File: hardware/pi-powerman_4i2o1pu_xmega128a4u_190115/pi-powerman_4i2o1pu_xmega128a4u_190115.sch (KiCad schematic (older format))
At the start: 93 parts, among them J1 Vin: +[16, 24]V, J2 UPS_in, J3 UPS_out, J4 AVR-PDI-6, J5 +5V OUT1, J7 +5V OUT2, J8 UPS_status, J9 UPS_bat, Q1 IRLML6402, Q2 BSS138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

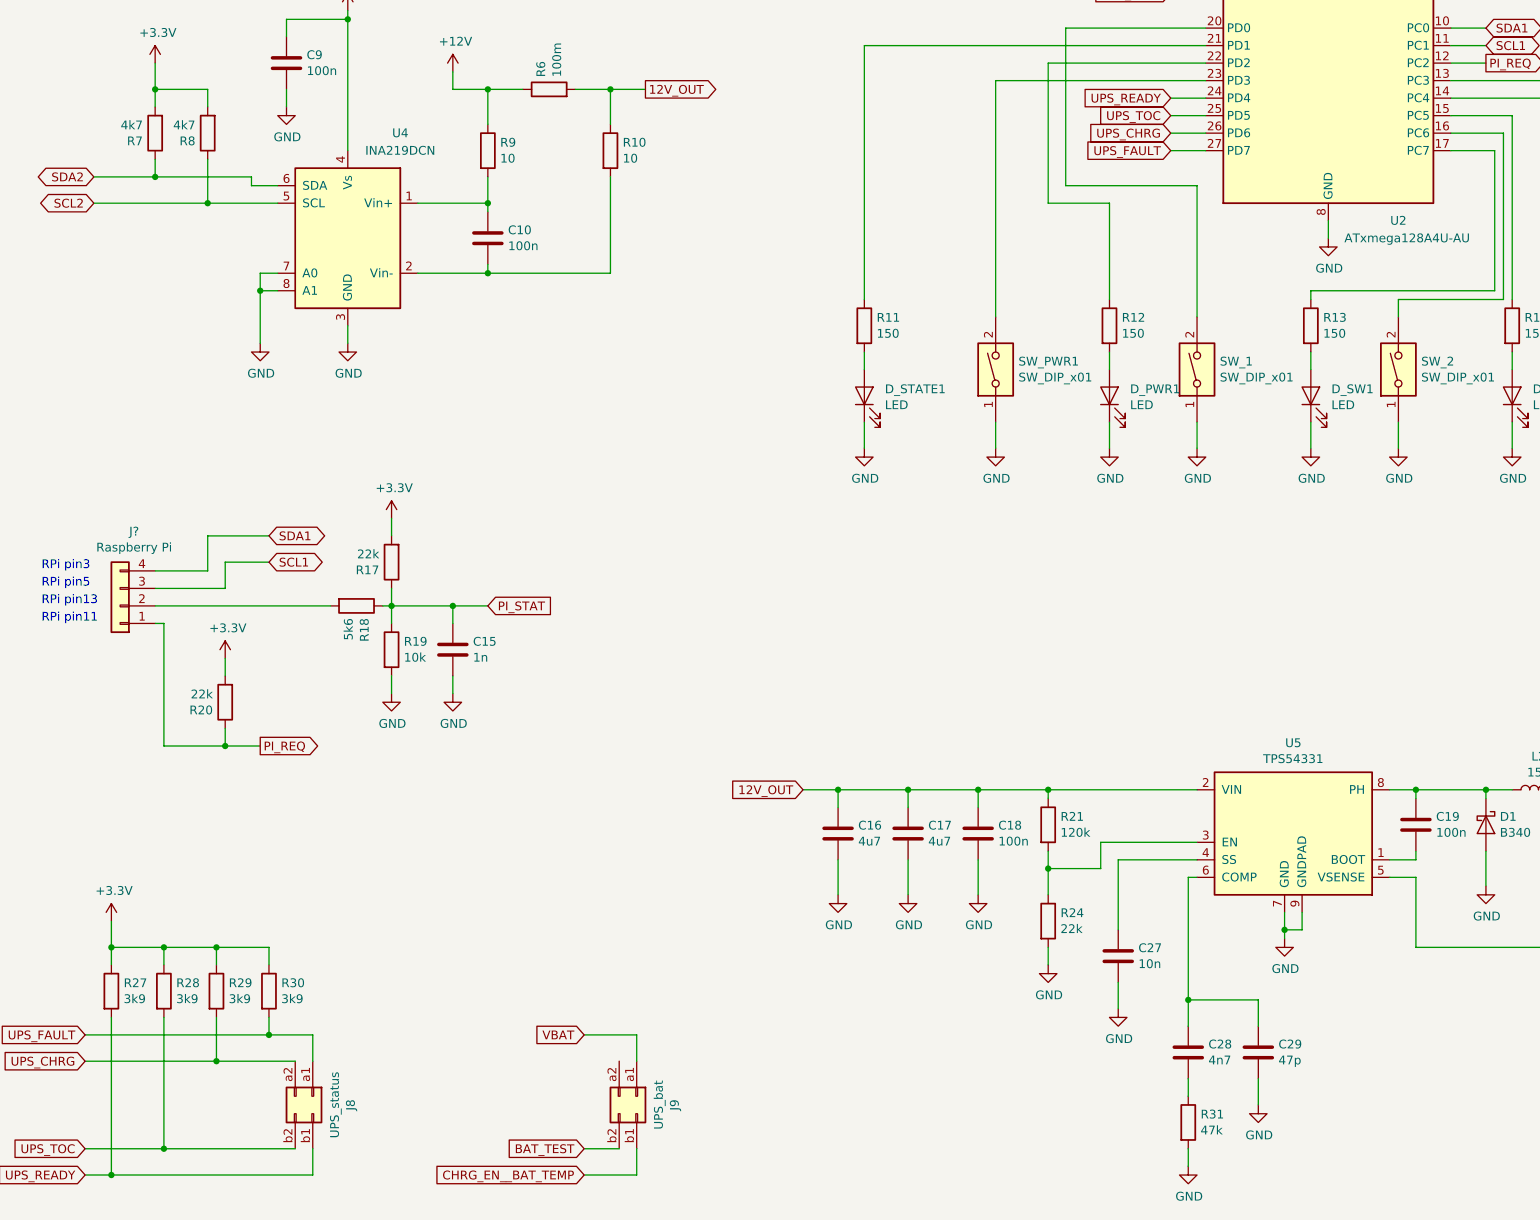
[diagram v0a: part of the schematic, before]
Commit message: symbols update
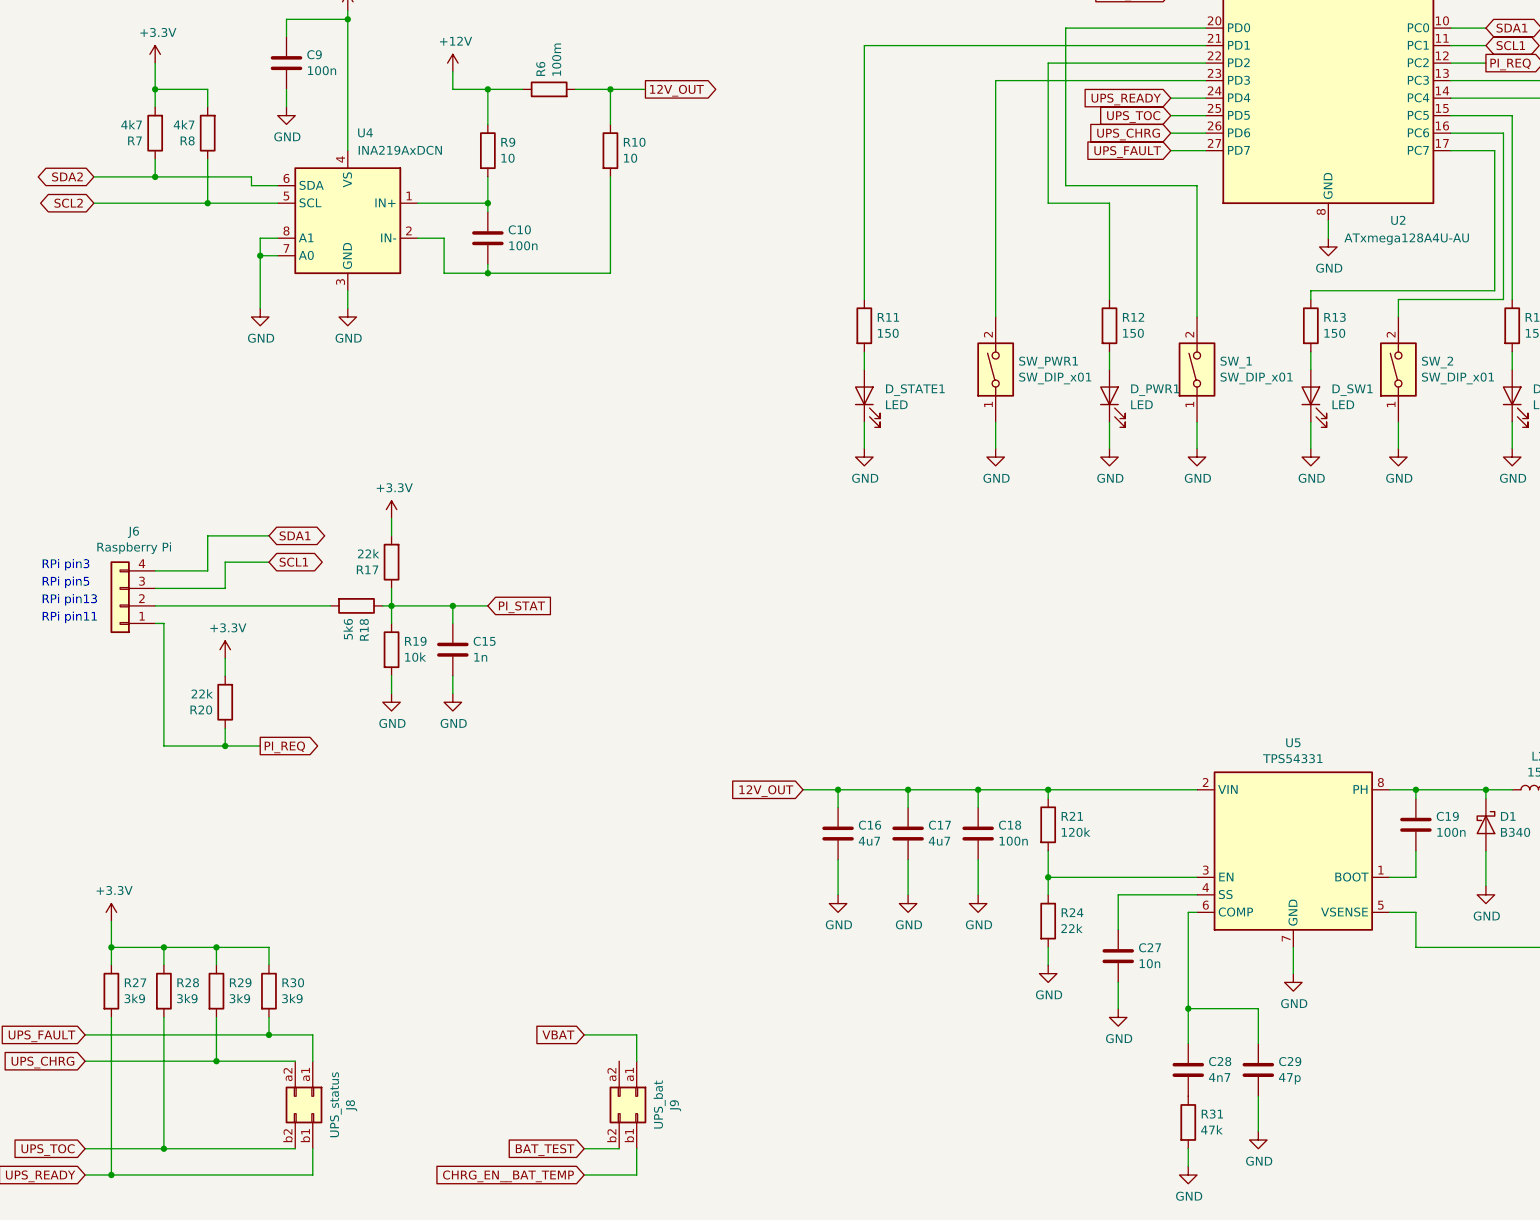
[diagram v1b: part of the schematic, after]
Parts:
- removed U4: INA219DCN, symbol ina219dcn:INA219DCN
- removed U5: TPS54331, symbol tps54331:TPS54331
- added U4: INA219AxDCN, Package_TO_SOT_SMD:SOT-23-8, symbol Analog_ADC:INA219AxDCN
- added U5: TPS54331, Package_SO:SOIC-8_3.9x4.9mm_P1.27mm, symbol obbo_IC:TPS54331
- U2: footprint Housings_QFP:TQFP-44_10x10mm_Pitch0.8mm -> Package_QFP:TQFP-44_10x10mm_P0.8mm
- gave numbers to parts that had none: 1
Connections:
- net +3V3: now also U4.4 (VS)
- net 12V_OUT: now also U5.2 (VIN)
- net GND: now also U4.3 (GND), U4.7 (A0), U4.8 (A1), U5.7 (GND)
- net SCL2: now also U4.5 (SCL)
- net SDA2: now also U4.6 (SDA)
- net at R23.2, R25.1, R26.1: now also U5.5 (VSENSE)
- net at C19.1, D1.1 (K), L2.1: now also U5.8 (PH)
- net at C19.2: now also U5.1 (BOOT)
- net at C28.1, C29.1: now also U5.6 (COMP)
- net at C27.1: now also U5.4 (SS)
- net at R21.2, R24.1: now also U5.3 (EN)
- net at C10.1, R9.2: now also U4.1 (IN+)
- net at C10.2, R10.2: now also U4.2 (IN-)
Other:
- moved on the sheet: C28, C29
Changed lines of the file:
@@
 EESchema Schematic File Version 4
 LIBS:pi-powerman_4i2o1pu_xmega128a4u_190115-cache
-EELAYER 26 0
+EELAYER 30 0
 EELAYER END
 $Descr A3 16535 11693
@@
 $EndDescr
 $Comp
-L MCU_Microchip_ATmega:ATxmega128A4U-AU U2
-U 1 1 5C9A9842
-P 8650 3550
-F 0 "U2" H 9050 2150 50  0000 C CNN
-F 1 "ATxmega128A4U-AU" H 9100 2050 50  0000 C CNN
-F 2 "Housings_QFP:TQFP-44_10x10mm_Pitch0.8mm" H 8650 3550 50  0001 C CIN
-F 3 "http://ww1.microchip.com/downloads/en/DeviceDoc/Atmel-8387-8-and16-bit-AVR-Microcontroller-XMEGA-A4U_Datasheet.pdf" H 8650 3550 50  0001 C CNN
-	1    8650 3550
-	1    0    0    -1
-$EndComp
-$Comp
 L Regulator_Linear:LM1117-3.3 U3
 U 1 1 5C9A9A34
@@
 L Device:C C29
 U 1 1 5C9AE2DB
-P 8250 9700
-F 0 "C29" H 8365 9746 50  0000 L CNN
-F 1 "47p" H 8365 9655 50  0000 L CNN
-F 2 "Resistors_SMD:R_0805_HandSoldering" H 8288 9550 50  0001 C CNN
-F 3 "~" H 8250 9700 50  0001 C CNN
-	1    8250 9700
+P 8250 9800
+F 0 "C29" H 8365 9846 50  0000 L CNN
+F 1 "47p" H 8365 9755 50  0000 L CNN
+F 2 "Resistors_SMD:R_0805_HandSoldering" H 8288 9650 50  0001 C CNN
+F 3 "~" H 8250 9800 50  0001 C CNN
+	1    8250 9800
 	1    0    0    -1
 $EndComp
@@
 L Device:C C28
 U 1 1 5C9AE33F
-P 7850 9700
-F 0 "C28" H 7965 9746 50  0000 L CNN
-F 1 "4n7" H 7965 9655 50  0000 L CNN
-F 2 "Resistors_SMD:R_0805_HandSoldering" H 7888 9550 50  0001 C CNN
-F 3 "~" H 7850 9700 50  0001 C CNN
-	1    7850 9700
+P 7850 9800
+F 0 "C28" H 7965 9846 50  0000 L CNN
+F 1 "4n7" H 7965 9755 50  0000 L CNN
+F 2 "Resistors_SMD:R_0805_HandSoldering" H 7888 9650 50  0001 C CNN
+F 3 "~" H 7850 9800 50  0001 C CNN
+	1    7850 9800
 	1    0    0    -1
 $EndComp
@@
 $EndComp
 $Comp
-L tps54331:TPS54331 U5
-U 1 1 5C9FF6F5
-P 8450 8400
-F 0 "U5" H 8450 8867 50  0000 C CNN
-F 1 "TPS54331" H 8450 8776 50  0000 C CNN
-F 2 "" H 8400 8400 50  0001 C CNN
-F 3 "" H 8400 8400 50  0001 C CNN
-	1    8450 8400
-	1    0    0    -1
-$EndComp
-$Comp
 L power:GND #PWR075
 U 1 1 5CA013F7
@@
 L power:GND #PWR070
 U 1 1 5CA0163B
-P 8400 9050
-F 0 "#PWR070" H 8400 8800 50  0001 C CNN
-F 1 "GND" H 8405 8877 50  0000 C CNN
-F 2 "" H 8400 9050 50  0001 C CNN
-F 3 "" H 8400 9050 50  0001 C CNN
-	1    8400 9050
+P 8450 9250
+F 0 "#PWR070" H 8450 9000 50  0001 C CNN
+F 1 "GND" H 8455 9077 50  0000 C CNN
+F 2 "" H 8450 9250 50  0001 C CNN
+F 3 "" H 8450 9250 50  0001 C CNN
+	1    8450 9250
 	1    0    0    -1
 $EndComp
@@
 L power:GND #PWR074
 U 1 1 5CA0168C
-P 8250 10000
-F 0 "#PWR074" H 8250 9750 50  0001 C CNN
-F 1 "GND" H 8255 9827 50  0000 C CNN
-F 2 "" H 8250 10000 50  0001 C CNN
-F 3 "" H 8250 10000 50  0001 C CNN
-	1    8250 10000
+P 8250 10150
+F 0 "#PWR074" H 8250 9900 50  0001 C CNN
+F 1 "GND" H 8255 9977 50  0000 C CNN
+F 2 "" H 8250 10150 50  0001 C CNN
+F 3 "" H 8250 10150 50  0001 C CNN
+	1    8250 10150
 	1    0    0    -1
 $EndComp
@@
 	7050 8200 6650 8200
 Wire Wire Line
-	7050 8550 7050 8650
+	7050 8550 7050 8700
 Wire Wire Line
 	7050 9100 7050 9200
@@
 Wire Wire Line
 	5850 8600 5850 8800
-Wire Wire Line
-	7900 8500 7350 8500
-Wire Wire Line
-	7350 8500 7350 8650
-Wire Wire Line
-	7350 8650 7050 8650
-Connection ~ 7050 8650
-Wire Wire Line
-	7050 8650 7050 8800
-Wire Wire Line
-	7900 8600 7450 8600
-Wire Wire Line
-	7450 8600 7450 9000
-Wire Wire Line
-	8250 9400 7850 9400
+Connection ~ 7050 8700
+Wire Wire Line
+	7050 8700 7050 8800
+Wire Wire Line
+	7900 8800 7450 8800
+Wire Wire Line
+	7450 8800 7450 9000
+Wire Wire Line
+	8250 9450 7850 9450
 Wire Wire Line
 	7450 9300 7450 9450
 Wire Wire Line
-	7850 9850 7850 9950
-Wire Wire Line
-	8250 9850 8250 10000
+	8250 9950 8250 10150
 Wire Wire Line
 	7850 10250 7850 10350
-Wire Wire Line
-	8400 8900 8400 9000
-Wire Wire Line
-	8500 8900 8500 9000
-Wire Wire Line
-	8500 9000 8400 9000
-Connection ~ 8400 9000
-Wire Wire Line
-	8400 9000 8400 9050
 Wire Wire Line
 	9000 8200 9150 8200
@@
 	9150 8200 9550 8200
 Wire Wire Line
-	9150 8550 9150 8600
-Wire Wire Line
-	9150 8600 9000 8600
+	9150 8550 9150 8700
+Wire Wire Line
+	9150 8700 9000 8700
 Wire Wire Line
 	9550 8550 9550 8750
@@
 	11100 9100 9150 9100
 Wire Wire Line
-	9150 9100 9150 8700
-Wire Wire Line
-	9150 8700 9000 8700
+	9150 9100 9150 8900
+Wire Wire Line
+	9150 8900 9000 8900
 Connection ~ 11250 9000
 $Comp
@@
 Wire Wire Line
 	1950 4200 1950 4050
-$Comp
-L ina219dcn:INA219DCN U4
-U 1 1 5CE81E04
-P 3050 5050
-F 0 "U4" H 3350 5650 50  0000 C CNN
-F 1 "INA219DCN" H 3350 5550 50  0000 C CNN
-F 2 "" H 3050 5050 50  0001 C CNN
-F 3 "" H 3050 5050 50  0001 C CNN
-	1    3050 5050
-	1    0    0    -1
-$EndComp
 Wire Wire Line
 	2250 4850 2650 4850
@@
 L power:GND #PWR033
 U 1 1 5CEC82A7
-P 3050 5650
-F 0 "#PWR033" H 3050 5400 50  0001 C CNN
-F 1 "GND" H 3055 5477 50  0000 C CNN
-F 2 "" H 3050 5650 50  0001 C CNN
-F 3 "" H 3050 5650 50  0001 C CNN
-	1    3050 5650
+P 3050 5450
+F 0 "#PWR033" H 3050 5200 50  0001 C CNN
+F 1 "GND" H 3055 5277 50  0000 C CNN
+F 2 "" H 3050 5450 50  0001 C CNN
+F 3 "" H 3050 5450 50  0001 C CNN
+	1    3050 5450
 	1    0    0    -1
 $EndComp
@@
 L power:GND #PWR032
 U 1 1 5CEF341C
-P 2550 5650
-F 0 "#PWR032" H 2550 5400 50  0001 C CNN
-F 1 "GND" H 2555 5477 50  0000 C CNN
-F 2 "" H 2550 5650 50  0001 C CNN
-F 3 "" H 2550 5650 50  0001 C CNN
-	1    2550 5650
+P 2550 5450
+F 0 "#PWR032" H 2550 5200 50  0001 C CNN
+F 1 "GND" H 2555 5277 50  0000 C CNN
+F 2 "" H 2550 5450 50  0001 C CNN
+F 3 "" H 2550 5450 50  0001 C CNN
+	1    2550 5450
 	1    0    0    -1
 $EndComp
@@
 	3050 3800 3050 3750
 Wire Wire Line
-	2550 5650 2550 5350
-Wire Wire Line
-	2550 5250 2650 5250
-Wire Wire Line
-	2650 5350 2550 5350
-Connection ~ 2550 5350
-Wire Wire Line
-	2550 5350 2550 5250
-Wire Wire Line
-	3050 5550 3050 5650
+	2550 5450 2550 5150
+Wire Wire Line
+	2550 5050 2650 5050
+Wire Wire Line
+	2650 5150 2550 5150
+Connection ~ 2550 5150
+Wire Wire Line
+	2550 5150 2550 5050
+Wire Wire Line
+	3050 5350 3050 5450
 $Comp
 L Device:C C10
@@
 	3850 4900 3850 4850
 Connection ~ 3850 4850
-Wire Wire Line
-	3450 5250 3850 5250
 Wire Wire Line
 	4550 5250 4550 4700
@@
 	8650 1150 8650 1100
 Wire Wire Line
-	7850 9400 7850 9550
-Connection ~ 7850 9400
-Wire Wire Line
-	8250 9400 8250 9550
-Wire Wire Line
-	7850 8700 7850 9400
-Wire Wire Line
-	7850 8700 7900 8700
+	7850 9450 7850 9650
+Connection ~ 7850 9450
+Wire Wire Line
+	8250 9450 8250 9650
+Wire Wire Line
+	7850 8900 7850 9450
+Wire Wire Line
+	7850 8900 7900 8900
 Wire Wire Line
 	3650 4100 3650 4200
@@
 Connection ~ 3850 4200
 $Comp
-L Connector_Generic:Conn_01x04 J?
+L Connector_Generic:Conn_01x04 J6
 U 1 1 5CB5CD3E
 P 1750 7150
-F 0 "J?" H 1670 6725 50  0000 C CNN
+F 0 "J6" H 1670 6725 50  0000 C CNN
 F 1 "Raspberry Pi" H 1670 6816 50  0000 C CNN
 F 2 "" H 1750 7150 50  0001 C CNN
@@
 Text Notes 1300 7250 0    50   ~ 0
 RPi pin11
+$Comp
+L Analog_ADC:INA219AxDCN U4
+U 1 1 5DDE89A8
+P 3050 4950
+F 0 "U4" H 2950 5450 50  0000 C CNN
+F 1 "INA219AxDCN" H 2750 5350 50  0000 C CNN
+F 2 "Package_TO_SOT_SMD:SOT-23-8" H 3700 4600 50  0001 C CNN
+F 3 "http://www.ti.com/lit/ds/symlink/ina219.pdf" H 3400 4850 50  0001 C CNN
+	1    3050 4950
+	-1   0    0    -1
+$EndComp
+Wire Wire Line
+	3450 5050 3600 5050
+Wire Wire Line
+	3600 5050 3600 5250
+Wire Wire Line
+	3600 5250 3850 5250
+$Comp
+L obbo_IC:TPS54331 U5
+U 1 1 5DE7FF98
+P 8450 8400
+F 0 "U5" H 8450 8867 50  0000 C CNN
+F 1 "TPS54331" H 8450 8776 50  0000 C CNN
+F 2 "Package_SO:SOIC-8_3.9x4.9mm_P1.27mm" H 9250 8850 50  0001 R CIN
+F 3 "http://www.ti.com/lit/ds/symlink/tps54331.pdf" H 8400 8400 50  0001 C CNN
+	1    8450 8400
+	1    0    0    -1
+$EndComp
+Wire Wire Line
+	7050 8700 7900 8700
+Wire Wire Line
+	8450 9100 8450 9250
+$Comp
+L MCU_Microchip_ATmega:ATxmega128A4U-AU U2
+U 1 1 5DE7BE9C
+P 8650 3550
+F 0 "U2" H 9050 2150 50  0000 C CNN
+F 1 "ATxmega128A4U-AU" H 9100 2050 50  0000 C CNN
+F 2 "Package_QFP:TQFP-44_10x10mm_P0.8mm" H 8650 3550 50  0001 C CIN
+F 3 "http://ww1.microchip.com/downloads/en/DeviceDoc/Atmel-8387-8-and16-bit-AVR-Microcontroller-XMEGA-A4U_Datasheet.pdf" H 8650 3550 50  0001 C CNN
+	1    8650 3550
+	1    0    0    -1
+$EndComp
 $EndSCHEMATC
